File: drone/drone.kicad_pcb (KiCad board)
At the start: 2 copper layers, 3 parts, among them U1 ESP32-WROOM-32, U2 MPU-6050, U3 DWM1000

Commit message: up pcb
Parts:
- added C1: C, Capacitor_SMD:C_0603_1608Metric, F.Cu at (105.4, 101.6)
- added C2: C, Capacitor_SMD:C_0603_1608Metric, F.Cu at (101.6, 105.4)
- added C3: C, Capacitor_SMD:C_0603_1608Metric, F.Cu at (107.0, 101.6)
- added C4: C, Resistor_SMD:R_0603_1608Metric, F.Cu at (96.3, 113.6)
- added C5: C, Resistor_SMD:R_0603_1608Metric, F.Cu at (97.9, 113.6)
- added D1: 1N5819, Diode_THT:D_DO-41_SOD81_P10.16mm_Horizontal, F.Cu at (78.6, 85.8)
- added D2: 1N5819, Diode_THT:D_DO-41_SOD81_P10.16mm_Horizontal, F.Cu at (78.6, 117.4)
- added D3: 1N5819, Diode_THT:D_DO-41_SOD81_P10.16mm_Horizontal, F.Cu at (117.1, 79.0)
- added D4: 1N5819, Diode_THT:D_DO-41_SOD81_P10.16mm_Horizontal, F.Cu at (117.4, 124.7)
- added J1: Conn_01x03, Connector_PinHeader_2.54mm:PinHeader_1x03_P2.54mm_Vertical, F.Cu at (99.1, 124.5)
- added J2: Conn_02x03_Top_Bottom, Connector_PinHeader_2.54mm:PinHeader_2x03_P2.54mm_Vertical, F.Cu at (80.0, 99.1)
- added J3: Conn_01x02, Connector_PinHeader_2.54mm:PinHeader_1x02_P2.54mm_Vertical, F.Cu at (78.8, 80.6)
- added J4: Conn_01x02, Connector_PinHeader_2.54mm:PinHeader_1x02_P2.54mm_Vertical, F.Cu at (78.9, 122.6)
- added J5: Conn_01x02, Connector_PinHeader_2.54mm:PinHeader_1x02_P2.54mm_Vertical, F.Cu at (121.9, 79.3)
- added J6: Conn_01x02, Connector_PinHeader_2.54mm:PinHeader_1x02_P2.54mm_Vertical, F.Cu at (122.6, 124.4)
- added Q1: Si2319CDS, Package_TO_SOT_SMD:SOT-23, F.Cu at (88.9, 82.5)
- added Q2: Si2319CDS, Package_TO_SOT_SMD:SOT-23, F.Cu at (88.9, 121.9)
- added Q3: Si2319CDS, Package_TO_SOT_SMD:SOT-23, F.Cu at (116.8, 83.8)
- added Q4: Si2319CDS, Package_TO_SOT_SMD:SOT-23, F.Cu at (120.7, 115.6)
- added R1: R_Small, Resistor_SMD:R_0603_1608Metric, F.Cu at (91.4, 100.3)
- added R2: R_Small, Resistor_SMD:R_0603_1608Metric, F.Cu at (89.2, 100.3)
- added R3: R_Small, Resistor_SMD:R_0603_1608Metric, F.Cu at (86.4, 86.4)
- added R4: R_Small, Resistor_SMD:R_0603_1608Metric, F.Cu at (91.5, 121.9)
- added R5: R_Small, Resistor_SMD:R_0603_1608Metric, F.Cu at (114.1, 83.8)
- added R6: R_Small, Resistor_SMD:R_0603_1608Metric, F.Cu at (117.9, 115.6)
- U1: value ESP32-WROOM-32 -> ATmega328P-A; footprint RF_Module:ESP32-WROOM-32 -> Package_QFP:TQFP-32_7x7mm_P0.8mm
- moved U3 67.8 mm to (124.5, 101.6), turned to -90 degrees
- moved U2 65.9 mm to (101.6, 101.6)
- moved U1 57.8 mm to (88.9, 113.0), turned to 180 degrees
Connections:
- U1 pad 1: Net-(U1-Pad1) -> MOTOR_4
- U1 pad 10: unconnected-(U1-Pad10) -> MOTOR_2
- U1 pad 12: unconnected-(U1-Pad12) -> MPU_IRQ
- U1 pad 13: unconnected-(U1-Pad13) -> MOTOR_3
- U1 pad 14: unconnected-(U1-Pad14) -> SS
- U1 pad 15: Net-(U1-Pad1) -> MOSI
- U1 pad 16: unconnected-(U1-Pad16) -> MISO
- U1 pad 17: unconnected-(U1-Pad17) -> SCK
- U1 pad 18: unconnected-(U1-Pad18) -> VCC
- U1 pad 21: unconnected-(U1-Pad21) -> GND
- U1 pad 26: unconnected-(U1-Pad26) -> DW_RST
- U1 pad 27: unconnected-(U1-Pad27) -> SDA
- U1 pad 28: unconnected-(U1-Pad28) -> SCL
- U1 pad 29: unconnected-(U1-Pad29) -> RST
- U1 pad 3: unconnected-(U1-Pad3) -> GND
- U1 pad 30: unconnected-(U1-Pad30) -> RX
- U1 pad 31: unconnected-(U1-Pad31) -> TX
- U1 pad 32: unconnected-(U1-Pad32) -> DW_IRQ
- U1 pad 4: unconnected-(U1-Pad4) -> VCC
- U1 pad 5: unconnected-(U1-Pad5) -> GND
- U1 pad 6: unconnected-(U1-Pad6) -> VCC
- U1 pad 9: unconnected-(U1-Pad9) -> MOTOR_1
- U2 pad 1: unconnected-(U2-Pad1) -> GND
- U2 pad 10: unconnected-(U2-Pad10) -> Net-(U2-Pad10)
- U2 pad 11: unconnected-(U2-Pad11) -> GND
- U2 pad 12: unconnected-(U2-Pad12) -> MPU_IRQ
- U2 pad 13: unconnected-(U2-Pad13) -> VCC
- U2 pad 18: unconnected-(U2-Pad18) -> GND
- U2 pad 20: unconnected-(U2-Pad20) -> Net-(U2-Pad20)
- U2 pad 23: unconnected-(U2-Pad23) -> SCL
- U2 pad 24: unconnected-(U2-Pad24) -> SDA
- U2 pad 8: unconnected-(U2-Pad8) -> VCC
- U2 pad 9: unconnected-(U2-Pad9) -> GND
- U3 pad 16: unconnected-(U3-Pad16) -> GND
- U3 pad 17: unconnected-(U3-Pad17) -> SS
- U3 pad 18: unconnected-(U3-Pad18) -> MOSI
- U3 pad 19: unconnected-(U3-Pad19) -> MISO
- U3 pad 20: unconnected-(U3-Pad20) -> SCK
- U3 pad 21: unconnected-(U3-Pad21) -> GND
- U3 pad 22: unconnected-(U3-Pad22) -> DW_IRQ
- U3 pad 23: unconnected-(U3-Pad23) -> GND
- U3 pad 24: unconnected-(U3-Pad24) -> GND
- U3 pad 3: unconnected-(U3-Pad3) -> DW_RST
- U3 pad 5: unconnected-(U3-Pad5) -> VCC
- U3 pad 6: unconnected-(U3-Pad6) -> VCC
- U3 pad 7: unconnected-(U3-Pad7) -> VCC
- U3 pad 8: unconnected-(U3-Pad8) -> GND
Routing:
- net VCC: track 0.00 -> 259.9 mm, vias 0 -> 5
- net SCK: track 0.00 -> 63.8 mm, vias 0 -> 4
- net MISO: track 0.00 -> 63.4 mm, vias 0 -> 2
- net DW_RST: track 0.00 -> 57.4 mm, vias 0 -> 2
- net MOSI: track 0.00 -> 49.0 mm, vias 0 -> 2
- net MOTOR_3: track 0.00 -> 46.9 mm, vias 0 -> 2
- net DW_IRQ: track 0.00 -> 35.2 mm
- net MOTOR_1: track 0.00 -> 33.8 mm, vias 0 -> 2
- net SS: track 0.00 -> 32.6 mm, vias 0 -> 2
- net SCL: track 0.00 -> 31.1 mm, vias 0 -> 2
- net SDA: track 0.00 -> 29.0 mm, vias 0 -> 2
- net MOTOR_4: track 0.00 -> 27.6 mm, vias 0 -> 2
- net RST: track 0.00 -> 24.9 mm, vias 0 -> 2
- net MPU_IRQ: track 0.00 -> 21.4 mm
- net MOTOR_2: track 0.00 -> 18.7 mm, vias 0 -> 2
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- added copper zone on B.Cu, net GND
- added copper zone on F.Cu, net GND
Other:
- board outline added: 50.8 x 50.8 mm

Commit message: add reamde
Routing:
- net GND: track 14.3 -> 15.9 mm
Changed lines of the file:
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@@
   (segment (start 97.81 100.35) (end 97.79 100.33) (width 0.25) (layer "F.Cu") (net 36))
   (segment (start 93.15 112.63) (end 95.3702 112.63) (width 0.25) (layer "F.Cu") (net 36))
+  (segment (start 84.65 113.43) (end 83.246836 113.43) (width 0.25) (layer "F.Cu") (net 36))
   (segment (start 99.65 100.35) (end 97.81 100.35) (width 0.25) (layer "F.Cu") (net 36))
   (segment (start 100.825 105.41) (end 101.35 104.885) (width 0.25) (layer "F.Cu") (net 36))
   (segment (start 102.35 103.55) (end 102.35 104.040685) (width 0.25) (layer "F.Cu") (net 36))
+  (segment (start 83.246836 113.43) (end 83.068375 113.608461) (width 0.25) (layer "F.Cu") (net 36))
   (segment (start 103.15 106.4) (end 102.87 106.68) (width 0.25) (layer "F.Cu") (net 36))
   (segment (start 93.91 114.23) (end 95.25 115.57) (width 0.25) (layer "F.Cu") (net 36))
@@
   (segment (start 84.6328 107.8992) (end 82.423 110.109) (width 0.25) (layer "B.Cu") (net 38))
   (segment (start 89.3826 115.4176) (end 89.3826 117.1974) (width 0.25) (layer "F.Cu") (net 39))
-  (segment (start 78.83 102.79) (end 78.83 112.231) (width 0.25) (layer "F.Cu") (net 39))
-  (segment (start 78.83 112.231) (end 81.915 115.316) (width 0.25) (layer "F.Cu") (net 39))
   (segment (start 89.3826 117.1974) (end 89.3 117.28) (width 0.25) (layer "F.Cu") (net 39))
-  (segment (start 80.005 101.615) (end 78.83 102.79) (width 0.25) (layer "F.Cu") (net 39))
+  (segment (start 78.83 102.79) (end 80.005 101.615) (width 0.25) (layer "F.Cu") (net 39))
+  (segment (start 78.83 112.231) (end 78.83 102.79) (width 0.25) (layer "F.Cu") (net 39))
+  (segment (start 81.28 114.681) (end 78.83 112.231) (width 0.25) (layer "F.Cu") (net 39))
+  (segment (start 81.28 115.316) (end 81.28 114.681) (width 0.25) (layer "F.Cu") (net 39))
   (via (at 89.3826 115.4176) (size 0.8) (drill 0.4) (layers "F.Cu" "B.Cu") (net 39))
-  (via (at 81.915 115.316) (size 0.8) (drill 0.4) (layers "F.Cu" "B.Cu") (net 39))
-  (segment (start 82.0166 115.4176) (end 89.3826 115.4176) (width 0.25) (layer "B.Cu") (net 39))
-  (segment (start 81.915 115.316) (end 82.0166 115.4176) (width 0.25) (layer "B.Cu") (net 39))
+  (via (at 81.28 115.316) (size 0.8) (drill 0.4) (layers "F.Cu" "B.Cu") (net 39))
+  (segment (start 81.3816 115.4176) (end 89.3826 115.4176) (width 0.25) (layer "B.Cu") (net 39))
+  (segment (start 81.28 115.316) (end 81.3816 115.4176) (width 0.25) (layer "B.Cu") (net 39))
   (segment (start 117.390235 124.681275) (end 115.91896 123.21) (width 0.4) (layer "F.Cu") (net 40))
   (segment (start 103.55 102.85) (end 104.985 102.85) (width 0.25) (layer "F.Cu") (net 40))
@@
   (segment (start 90.6526 104.4956) (end 87.4739 101.3169) (width 0.25) (layer "F.Cu") (net 40))
   (segment (start 95.3638 114.4138) (end 94.38 113.43) (width 0.25) (layer "F.Cu") (net 40))
-  (segment (start 83.205 111.105) (end 82.55 111.76) (width 0.25) (layer "F.Cu") (net 40))
   (segment (start 91.656852 110.36615) (end 91.656852 112.000348) (width 0.25) (layer "F.Cu") (net 40))
+  (segment (start 82.044987 117.345013) (end 82.011634 117.378366) (width 0.25) (layer "F.Cu") (net 40))
   (segment (start 94.38 113.43) (end 93.15 113.43) (width 0.25) (layer "F.Cu") (net 40))
   (segment (start 117.057898 78.957898) (end 115.242492 77.142492) (width 0.4) (layer "F.Cu") (net 40))
   (segment (start 78.642492 80.760244) (end 78.837057 80.565679) (width 0.4) (layer "F.Cu") (net 40))
-  (segment (start 84.65 111.03) (end 83.6 111.03) (width 0.25) (layer "F.Cu") (net 40))
-  (segment (start 83.6 111.03) (end 83.525 111.105) (width 0.25) (layer "F.Cu") (net 40))
   (segment (start 91.8272 111.83) (end 91.4908 112.1664) (width 0.25) (layer "F.Cu") (net 40))
   (segment (start 106.167663 104.521) (end 105.8926 104.521) (width 0.25) (layer "F.Cu") (net 40))
@@
   (segment (start 119.6588 97.435) (end 119.6588 95.3) (width 0.25) (layer "F.Cu") (net 40))
   (segment (start 117.3557 79.2557) (end 117.057898 78.957898) (width 0.4) (layer "F.Cu") (net 40))
+  (segment (start 82.044987 112.265013) (end 82.044987 117.345013) (width 0.25) (layer "F.Cu") (net 40))
   (segment (start 78.580684 117.378366) (end 78.580684 112.870684) (width 0.4) (layer "F.Cu") (net 40))
   (segment (start 106.205996 97.975) (end 107.6706 99.439604) (width 0.25) (layer "F.Cu") (net 40))
+  (segment (start 83.205 111.105) (end 82.044987 112.265013) (width 0.25) (layer "F.Cu") (net 40))
   (segment (start 115.242492 77.142492) (end 80.337508 77.142492) (width 0.4) (layer "F.Cu") (net 40))
-  (segment (start 82.55 111.76) (end 82.64 111.85) (width 0.25) (layer "F.Cu") (net 40))
   (segment (start 77.47 96.52) (end 77.47 86.999189) (width 0.4) (layer "F.Cu") (net 40))
   (segment (start 100.85 104.3566) (end 100.711 104.4956) (width 0.25) (layer "F.Cu") (net 40))
-  (segment (start 82.64 111.85) (end 82.64 116.75) (width 0.25) (layer "F.Cu") (net 40))
-  (segment (start 82.011634 117.378366) (end 78.580684 117.378366) (width 0.25) (layer "F.Cu") (net 40))
   (segment (start 116.8588 95.3) (end 116.8588 97.6818) (width 0.25) (layer "F.Cu") (net 40))
   (segment (start 82.7278 96.52) (end 77.47 96.52) (width 0.25) (layer "F.Cu") (net 40))
   (segment (start 78.74 78.74) (end 78.837057 78.837057) (width 0.4) (layer "F.Cu") (net 40))
   (segment (start 122.644025 124.436286) (end 117.635224 124.436286) (width 0.4) (layer "F.Cu") (net 40))
-  (segment (start 83.525 111.105) (end 83.205 111.105) (width 0.25) (layer "F.Cu") (net 40))
   (segment (start 91.4908 113.0046) (end 91.9162 113.43) (width 0.25) (layer "F.Cu") (net 40))
+  (segment (start 83.6 111.03) (end 83.525 111.105) (width 0.25) (layer "F.Cu") (net 40))
   (segment (start 100.711 104.4956) (end 90.6526 104.4956) (width 0.25) (layer "F.Cu") (net 40))
   (segment (start 85.7 111.03) (end 86.1755 111.5055) (width 0.25) (layer "F.Cu") (net 40))
@@
   (segment (start 95.508205 114.409595) (end 95.504 114.4138) (width 0.25) (layer "F.Cu") (net 40))
   (segment (start 87.4739 101.3169) (end 87.4739 101.2661) (width 0.25) (layer "F.Cu") (net 40))
-  (segment (start 82.64 116.75) (end 82.011634 117.378366) (width 0.25) (layer "F.Cu") (net 40))
   (segment (start 91.656852 112.000348) (end 91.4908 112.1664) (width 0.25) (layer "F.Cu") (net 40))
   (segment (start 87.125 101.615) (end 87.4739 101.2661) (width 0.25) (layer "F.Cu") (net 40))
   (segment (start 78.580684 112.870684) (end 77.47 111.76) (width 0.4) (layer "F.Cu") (net 40))
+  (segment (start 82.011634 117.378366) (end 78.580684 117.378366) (width 0.25) (layer "F.Cu") (net 40))
   (segment (start 78.858992 117.656674) (end 78.580684 117.378366) (width 0.4) (layer "F.Cu") (net 40))
+  (segment (start 83.525 111.105) (end 83.205 111.105) (width 0.25) (layer "F.Cu") (net 40))
   (segment (start 116.6876 100.4062) (end 116.6876 100.457) (width 0.25) (layer "F.Cu") (net 40))
   (segment (start 101.522919 98.45) (end 101.997919 97.975) (width 0.25) (layer "F.Cu") (net 40))
@@
   (segment (start 100.85 103.55) (end 100.85 104.3566) (width 0.25) (layer "F.Cu") (net 40))
   (segment (start 106.68 125.73) (end 90.17 125.73) (width 0.4) (layer "F.Cu") (net 40))
+  (segment (start 84.65 111.03) (end 83.6 111.03) (width 0.25) (layer "F.Cu") (net 40))
   (segment (start 82.545 101.615) (end 87.125 101.615) (width 0.25) (layer "F.Cu") (net 40))
   (segment (start 101.997919 97.975) (end 106.205996 97.975) (width 0.25) (layer "F.Cu") (net 40))

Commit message: up readme
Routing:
- net GND: track 15.9 -> 18.2 mm
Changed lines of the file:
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@@
   (segment (start 100.825 105.41) (end 101.35 104.885) (width 0.25) (layer "F.Cu") (net 36))
   (segment (start 102.35 103.55) (end 102.35 104.040685) (width 0.25) (layer "F.Cu") (net 36))
+  (segment (start 106.971935 102.386935) (end 105.41 100.825) (width 0.25) (layer "F.Cu") (net 36))
   (segment (start 83.246836 113.43) (end 83.068375 113.608461) (width 0.25) (layer "F.Cu") (net 36))
   (segment (start 103.15 106.4) (end 102.87 106.68) (width 0.25) (layer "F.Cu") (net 36))
   (segment (start 93.91 114.23) (end 95.25 115.57) (width 0.25) (layer "F.Cu") (net 36))
+  (segment (start 107.048911 102.386935) (end 106.971935 102.386935) (width 0.25) (layer "F.Cu") (net 36))
   (segment (start 93.15 114.23) (end 93.91 114.23) (width 0.25) (layer "F.Cu") (net 36))
   (segment (start 101.35 104.885) (end 101.35 103.55) (width 0.25) (layer "F.Cu") (net 36))

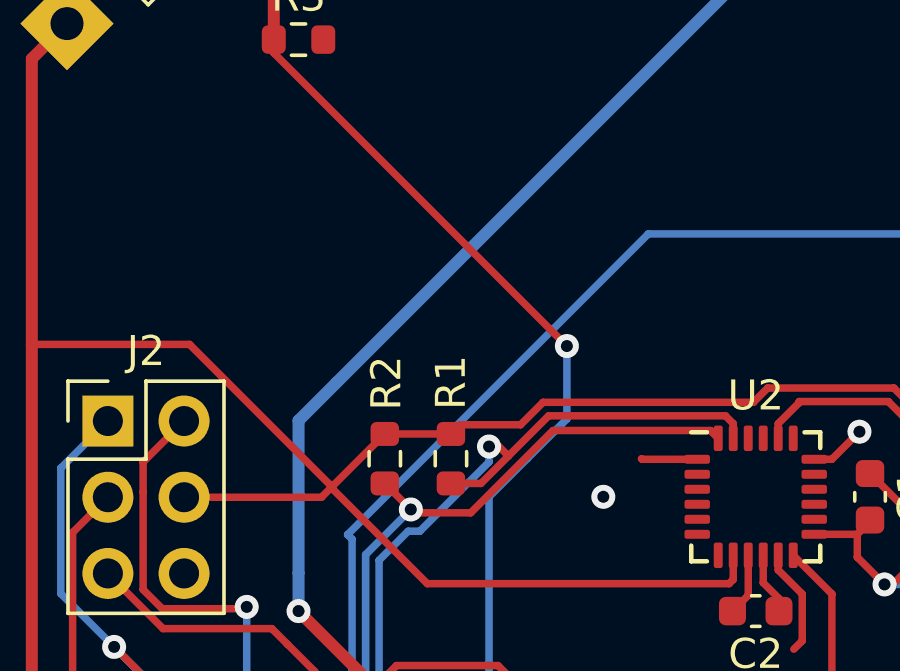
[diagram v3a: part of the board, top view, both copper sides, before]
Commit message: add drone BMP280
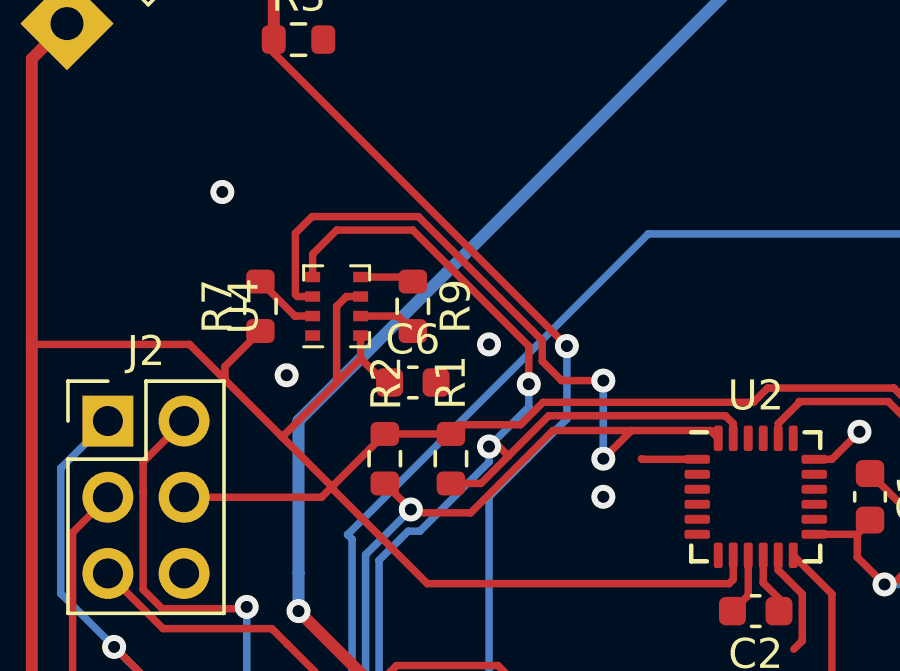
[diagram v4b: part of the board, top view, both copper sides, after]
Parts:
- added C6: C, Capacitor_SMD:C_0603_1608Metric, F.Cu at (90.2, 97.8)
- added R7: 10K, Resistor_SMD:R_0603_1608Metric, F.Cu at (85.1, 95.2)
- added R9: 10K, Resistor_SMD:R_0603_1608Metric, F.Cu at (90.2, 95.2)
- added U4: BMP280, Package_LGA:Bosch_LGA-8_2x2.5mm_P0.65mm_ClockwisePinNumbering, F.Cu at (87.6, 95.2)
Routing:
- net SDA: track 29.0 -> 48.8 mm, vias 2 -> 4
- net SCL: track 31.1 -> 44.9 mm, vias 2 -> 3
- net VCC: track 259.9 -> 271.2 mm
- net Net-(R7-Pad2): track 0.00 -> 2.22 mm
- net GND: track 18.2 -> 20.2 mm, vias 6 -> 9
- net Net-(R9-Pad1): track 0.00 -> 1.80 mm
